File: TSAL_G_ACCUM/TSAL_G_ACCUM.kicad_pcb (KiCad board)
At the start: 2 copper layers, 83.2 x 60 mm, 64 parts, among them J1 Conn_01x02_Pin, J11 Conn_01x02_Pin, J2 Conn_01x02_Pin, J3 Conn_01x02_Pin, J4 Conn_01x02_Pin, J5 Conn_01x02_Pin, J6 Conn_01x02_Pin, J7 Conn_01x03_Pin, U1 TLV431, U3 LTV-817S, U4 B1212, U5 uA7805, U6 LM393, U7 LM393, U8 LM393

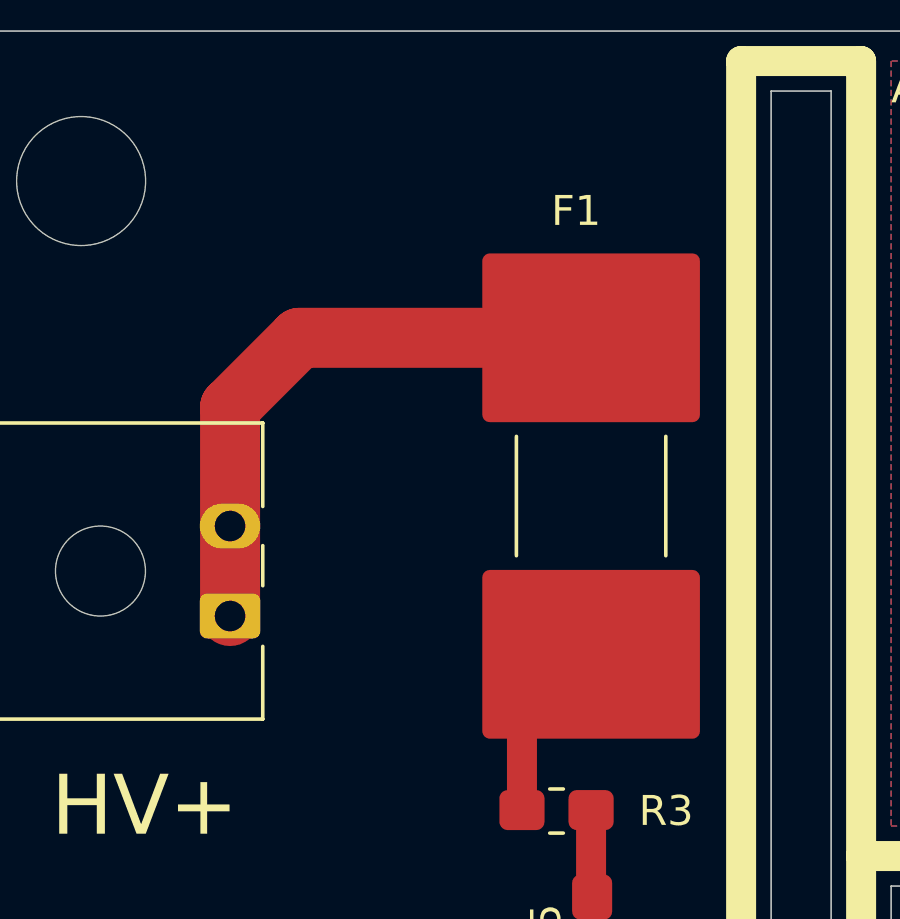
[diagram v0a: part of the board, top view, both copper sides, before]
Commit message: Increase HV and LVS Air distance
tsal g accum increase ts+ fuse distance to lvs  to comply the rule (or make it more obvious that it is complying the rule)
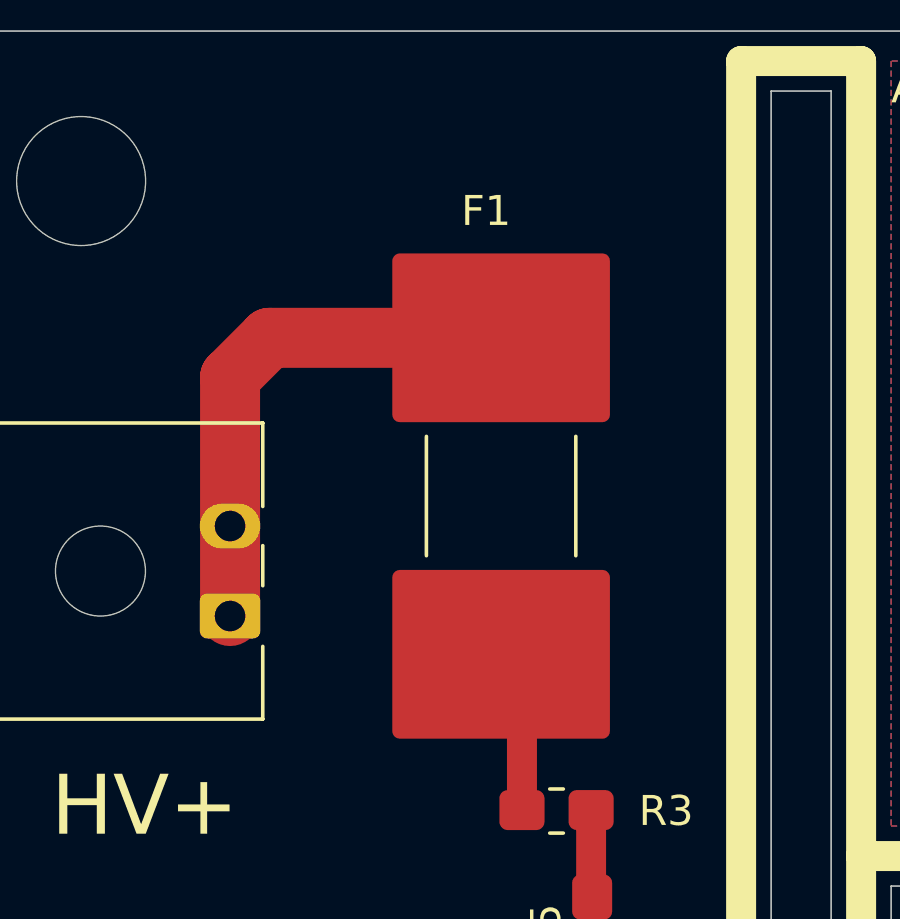
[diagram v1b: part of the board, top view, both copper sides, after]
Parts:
- moved F1 3.00 mm to (95.0, 84.5)
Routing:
- net Net-(J1-Pin_1): track 20.0 -> 17.5 mm
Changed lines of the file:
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@@
 	(footprint "Fuse:Fuse_Littelfuse-NANO2-885"
 		(layer "F.Cu")
-		(at 98 84.5 90)
+		(at 95 84.5 90)
 		(descr "Littelfuse NANO2, 350VAC, 450/500VDC, 10.86 x 4.78 x 4.78mm, https://www.littelfuse.com/media?resourcetype=datasheets&itemid=888f12ed-ed3b-4b45-b910-06af8854ad76&filename=littelfuse-fuse-885-datasheet")
 		(tags "Fuse Nano2 885")
@@
 	)
 	(segment
-		(start 85.965 85.5)
-		(end 85.965 81.535)
+		(start 85.965 80.535)
+		(end 87.275 79.225)
 		(width 2)
 		(layer "F.Cu")
@@
 	)
 	(segment
-		(start 85.965 81.535)
-		(end 88.275 79.225)
+		(start 85.965 85.5)
+		(end 85.965 80.535)
 		(width 2)
 		(layer "F.Cu")
@@
 	)
 	(segment
-		(start 88.275 79.225)
-		(end 98 79.225)
+		(start 87.275 79.225)
+		(end 95 79.225)
 		(width 2)
 		(layer "F.Cu")

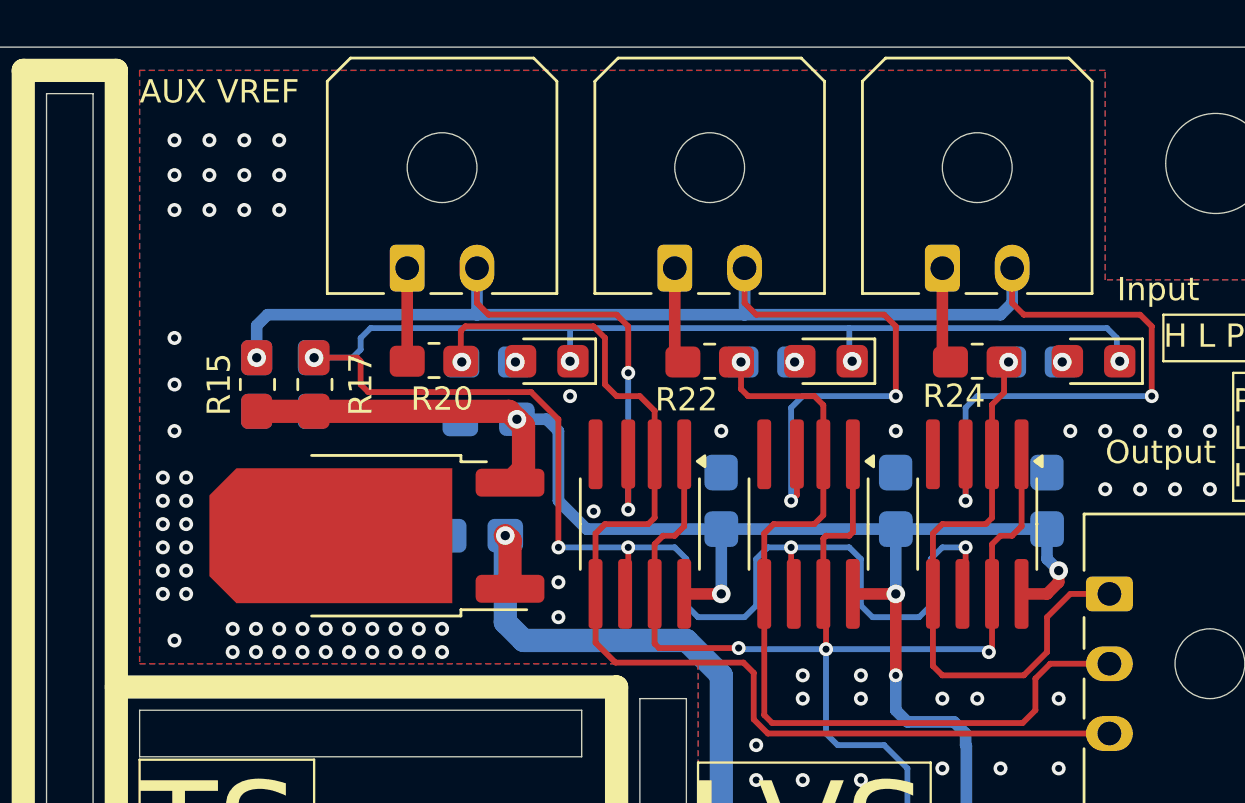
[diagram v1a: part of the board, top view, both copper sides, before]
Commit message: TSAl G ACCUM minor change
increased air distance from HV to LVS in pcb
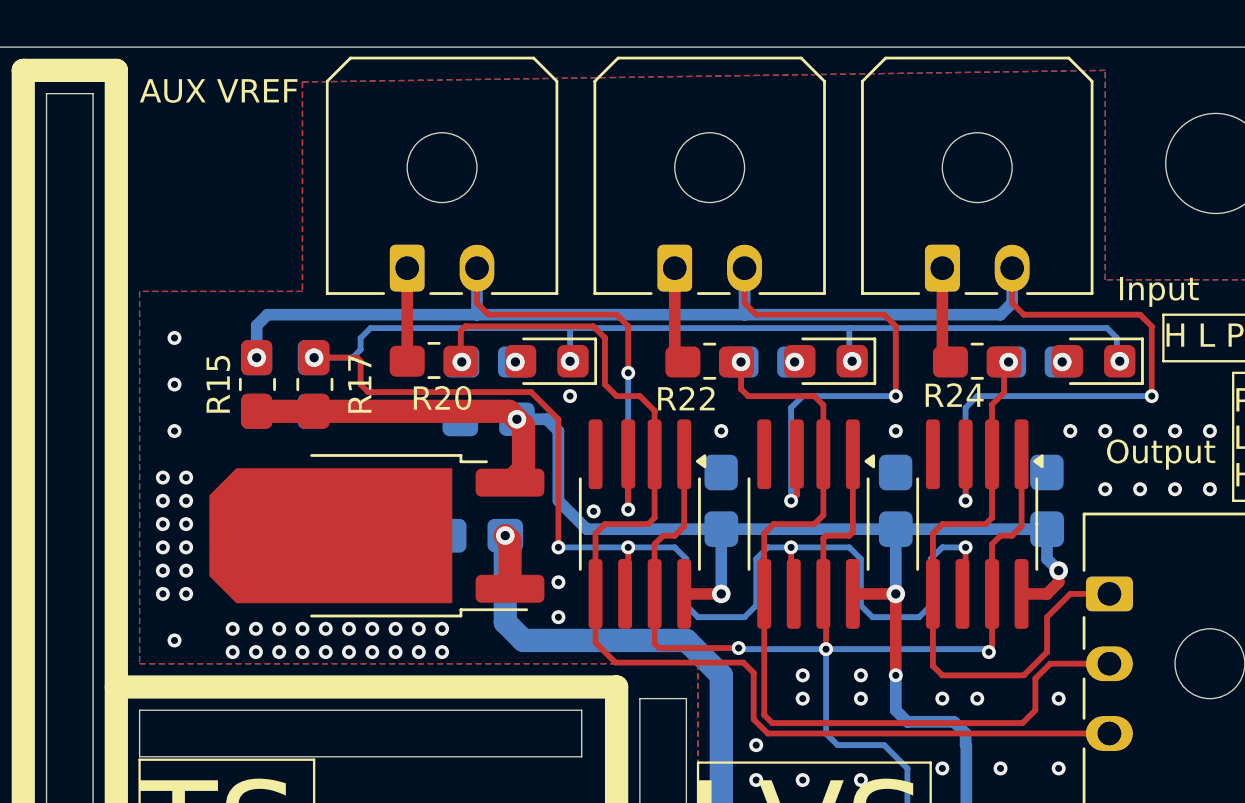
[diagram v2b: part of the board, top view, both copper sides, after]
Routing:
- net GLV-: vias 97 -> 85
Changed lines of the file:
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@@
-	)
-	(via
-		(at 111 74.5)
-		(size 0.6)
-		(drill 0.3)
-		(layers "F.Cu" "B.Cu")
-		(free yes)
-		(net 6)
-	)
-	(via
-		(at 111 73)
-		(size 0.6)
-		(drill 0.3)
-		(layers "F.Cu" "B.Cu")
-		(free yes)
-		(net 6)
 	)
 	(via
@@
 	)
 	(via
-		(at 109.5 74.5)
-		(size 0.6)
-		(drill 0.3)
-		(layers "F.Cu" "B.Cu")
-		(free yes)
-		(net 6)
-	)
-	(via
 		(at 140.5 108)
 		(size 0.6)
@@
 	)
 	(via
-		(at 112.5 74.5)
-		(size 0.6)
-		(drill 0.3)
-		(layers "F.Cu" "B.Cu")
-		(free yes)
-		(net 6)
-	)
-	(via
 		(at 151 85.5)
 		(size 0.6)
@@
 	)
 	(via
-		(at 114 73)
-		(size 0.6)
-		(drill 0.3)
-		(layers "F.Cu" "B.Cu")
-		(free yes)
-		(net 6)
-	)
-	(via
-		(at 112.5 73)
-		(size 0.6)
-		(drill 0.3)
-		(layers "F.Cu" "B.Cu")
-		(free yes)
-		(net 6)
-	)
-	(via
 		(at 109 87.5)
 		(size 0.6)
@@
 	)
 	(via
-		(at 114 76)
-		(size 0.6)
-		(drill 0.3)
-		(layers "F.Cu" "B.Cu")
-		(free yes)
-		(net 6)
-	)
-	(via
 		(at 150 114.5)
 		(size 0.6)
@@
 	)
 	(via
-		(at 109.5 76)
-		(size 0.6)
-		(drill 0.3)
-		(layers "F.Cu" "B.Cu")
-		(free yes)
-		(net 6)
-	)
-	(via
 		(at 154 88)
 		(size 0.6)
@@
 	)
 	(via
-		(at 114 74.5)
-		(size 0.6)
-		(drill 0.3)
-		(layers "F.Cu" "B.Cu")
-		(free yes)
-		(net 6)
-	)
-	(via
 		(at 133 126)
 		(size 0.6)
@@
 	)
 	(via
-		(at 109.5 73)
-		(size 0.6)
-		(drill 0.3)
-		(layers "F.Cu" "B.Cu")
-		(free yes)
-		(net 6)
-	)
-	(via
 		(at 136.5 100.5)
 		(size 0.6)
@@
 	)
 	(via
-		(at 111 76)
-		(size 0.6)
-		(drill 0.3)
-		(layers "F.Cu" "B.Cu")
-		(free yes)
-		(net 6)
-	)
-	(via
 		(at 136.5 96)
 		(size 0.6)
@@
 	(via
 		(at 134.5 99)
-		(size 0.6)
-		(drill 0.3)
-		(layers "F.Cu" "B.Cu")
-		(free yes)
-		(net 6)
-	)
-	(via
-		(at 112.5 76)
 		(size 0.6)
 		(drill 0.3)
@@
 		(polygon
 			(pts
-				(xy 149 128) (xy 149 119) (xy 159 119) (xy 158.5 79) (xy 149.5 79) (xy 149.5 70) (xy 108 70) (xy 108 95.5)
-				(xy 132 95.5) (xy 132 104.5) (xy 137 104.5) (xy 137 111.5) (xy 132 111.5) (xy 132 128)
+				(xy 149 128) (xy 149 119) (xy 159 119) (xy 158.5 79) (xy 149.5 79) (xy 149.5 70) (xy 115 70.5) (xy 115 79.5)
+				(xy 108 79.5) (xy 108 95.5) (xy 132 95.5) (xy 132 104.5) (xy 137 104.5) (xy 137 111.5) (xy 132 111.5)
+				(xy 132 128)
 			)
 		)
